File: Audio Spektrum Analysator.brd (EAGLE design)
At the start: 144.8 x 98.7 mm, 148 parts, among them IC1 LM324N, IC10 LM3914N, IC11 LM3914N, IC12 LM3914N, IC13 LM3914N, IC2 LM324N, IC3 LM324N, IC4 LM3914N, IC5 LM3914N, IC6 LM3914N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

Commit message: moved names
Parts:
- removed R8: 1k, rcl:0207/7
- removed R9: 1k, resistor:0207/7
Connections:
- removed net N$31: R10.S, R8.2
- removed net N$44: R11.S, R9.2
- net N$123: now also R11.S; no longer R9.1
- net N$5: now also R10.S; no longer R8.1
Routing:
- net N$44: track 6.88 -> 0.00 mm
- net N$31: track 6.88 -> 0.00 mm
- net N$5: track 8.15 -> 4.34 mm
- net N$123: track 6.35 -> 2.54 mm
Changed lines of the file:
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@@
 <layer number="25" name="tNames" color="7" fill="1" visible="yes" active="yes"/>
 <layer number="26" name="bNames" color="7" fill="1" visible="yes" active="yes"/>
-<layer number="27" name="tValues" color="7" fill="1" visible="yes" active="yes"/>
-<layer number="28" name="bValues" color="7" fill="1" visible="yes" active="yes"/>
+<layer number="27" name="tValues" color="7" fill="1" visible="no" active="yes"/>
+<layer number="28" name="bValues" color="7" fill="1" visible="no" active="yes"/>
 <layer number="29" name="tStop" color="7" fill="3" visible="no" active="yes"/>
 <layer number="30" name="bStop" color="7" fill="6" visible="no" active="yes"/>
@@
 <rectangle x1="134.127" y1="76.406" x2="134.787" y2="76.466" layer="26"/>
 <rectangle x1="134.127" y1="76.466" x2="134.787" y2="76.526" layer="26"/>
-<text x="1.27" y="0.762" size="1.778" layer="25" font="vector">5V</text>
+<text x="2.54" y="0.762" size="1.778" layer="25" font="vector">5V</text>
 </plain>
 <attributes>
@@
 <attribute name="VALUE" x="51.3588" y="4.064" size="1.27" layer="27" font="vector" ratio="10" rot="R90"/>
 </element>
-<element name="R9" library="resistor" library_urn="urn:adsk.eagle:library:348" package="0207/7" package3d_urn="urn:adsk.eagle:package:23493/1" value="1k" x="54.61" y="6.35" smashed="yes" rot="R270">
-<attribute name="NAME" x="55.626" y="10.922" size="1.27" layer="25" font="vector" ratio="10"/>
-<attribute name="VALUE" x="54.0512" y="8.636" size="1.27" layer="27" font="vector" ratio="10" rot="R270"/>
-</element>
 <element name="R17" library="resistor" library_urn="urn:adsk.eagle:library:348" package="0207/7" package3d_urn="urn:adsk.eagle:package:23493/1" value="1M" x="55.88" y="24.13" smashed="yes">
 <attribute name="NAME" x="53.34" y="25.527" size="1.27" layer="25" font="vector" ratio="10"/>
@@
 <attribute name="VALUE" x="107.2388" y="24.384" size="1.27" layer="27" font="vector" ratio="10" rot="R90"/>
 </element>
-<element name="R8" library="rcl" library_urn="urn:adsk.eagle:library:334" package="0207/7" package3d_urn="urn:adsk.eagle:package:23493/1" value="1k" x="34.29" y="6.35" smashed="yes" rot="R270">
-<attribute name="NAME" x="32.131" y="11.049" size="1.27" layer="25" font="vector" ratio="10"/>
-<attribute name="SPICEPREFIX" value="R" x="34.29" y="6.35" size="1.778" layer="27" rot="R270" display="off"/>
-<attribute name="VALUE" x="33.7312" y="8.636" size="1.27" layer="27" font="vector" ratio="10" rot="R270"/>
-</element>
 <element name="R47" library="resistor" library_urn="urn:adsk.eagle:library:348" package="0207/7" package3d_urn="urn:adsk.eagle:package:23493/1" value="1k2" x="43.815" y="57.15" smashed="yes" rot="R270">
 <attribute name="NAME" x="44.45" y="62.23" size="1.27" layer="25" font="vector" ratio="10" rot="R90"/>
@@
 <signal name="N$5">
 <contactref element="R6" pad="2"/>
-<contactref element="R8" pad="1"/>
 <contactref element="IC1" pad="2"/>
 <wire x1="40.64" y1="12.7" x2="40.64" y2="11.43" width="0.4064" layer="1"/>
 <wire x1="40.64" y1="11.43" x2="39.37" y2="10.16" width="0.4064" layer="1"/>
 <wire x1="39.37" y1="10.16" x2="38.1" y2="10.16" width="0.4064" layer="1"/>
-<wire x1="38.1" y1="10.16" x2="34.29" y2="10.16" width="0.4064" layer="1"/>
+<contactref element="R10" pad="S"/>
+<wire x1="27.94" y1="3.81" x2="38.1" y2="10.16" width="0" layer="19" extent="1-1"/>
 </signal>
 <signal name="N$6">
@@
 <contactref element="IC1" pad="6"/>
 <contactref element="R7" pad="2"/>
-<contactref element="R9" pad="1"/>
 <wire x1="50.8" y1="12.7" x2="50.8" y2="10.16" width="0.4064" layer="1"/>
-<wire x1="50.8" y1="10.16" x2="54.61" y2="10.16" width="0.4064" layer="1"/>
+<contactref element="R11" pad="S"/>
+<wire x1="50.8" y1="10.16" x2="60.96" y2="3.81" width="0" layer="19" extent="1-1"/>
 </signal>
 <signal name="REF">
@@
 <wire x1="20.32" y1="11.43" x2="20.32" y2="13.97" width="0.4064" layer="1"/>
 </signal>
-<signal name="N$31">
-<contactref element="R8" pad="2"/>
-<contactref element="R10" pad="S"/>
-<wire x1="27.94" y1="3.81" x2="29.21" y2="2.54" width="0.4064" layer="1"/>
-<wire x1="29.21" y1="2.54" x2="34.29" y2="2.54" width="0.4064" layer="1"/>
-</signal>
-<signal name="N$44">
-<contactref element="R9" pad="2"/>
-<contactref element="R11" pad="S"/>
-<wire x1="54.61" y1="2.54" x2="59.69" y2="2.54" width="0.4064" layer="1"/>
-<wire x1="59.69" y1="2.54" x2="60.96" y2="3.81" width="0.4064" layer="1"/>
-</signal>
 </signals>

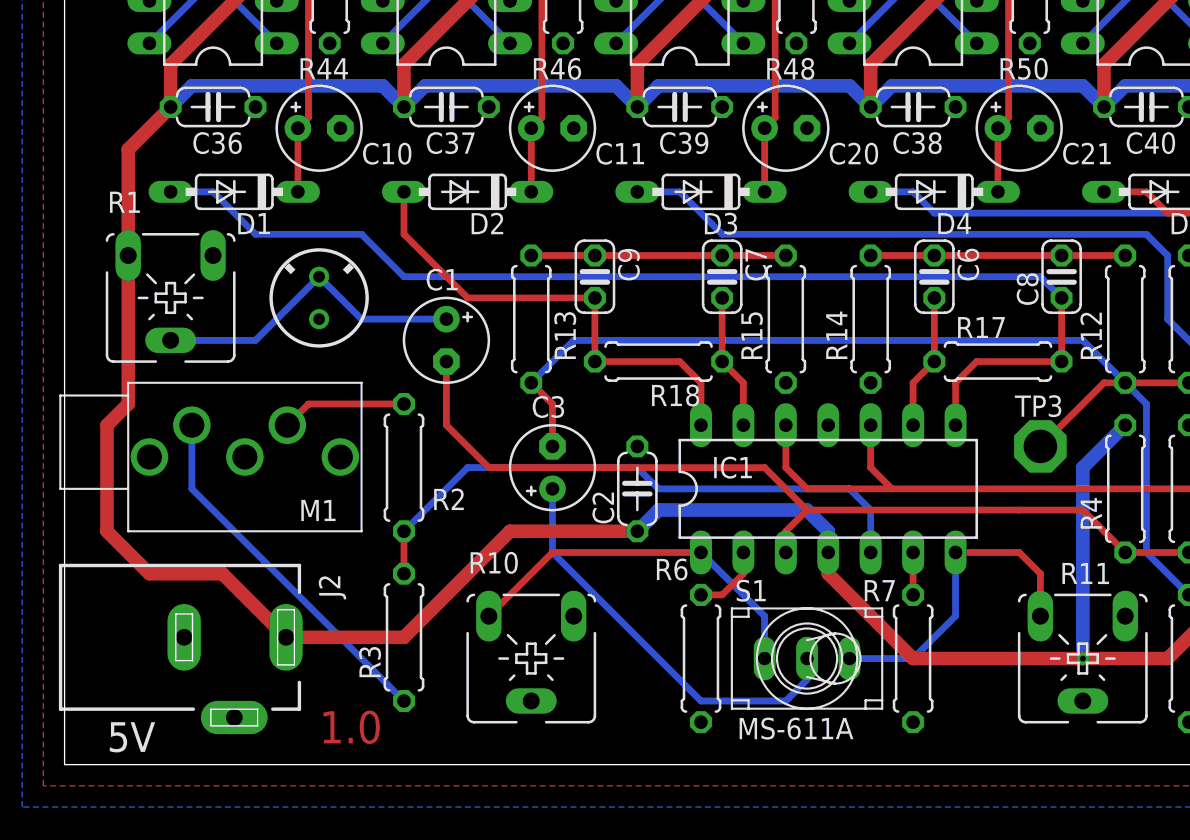
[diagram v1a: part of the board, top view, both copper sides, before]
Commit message: worked on electret mic amp
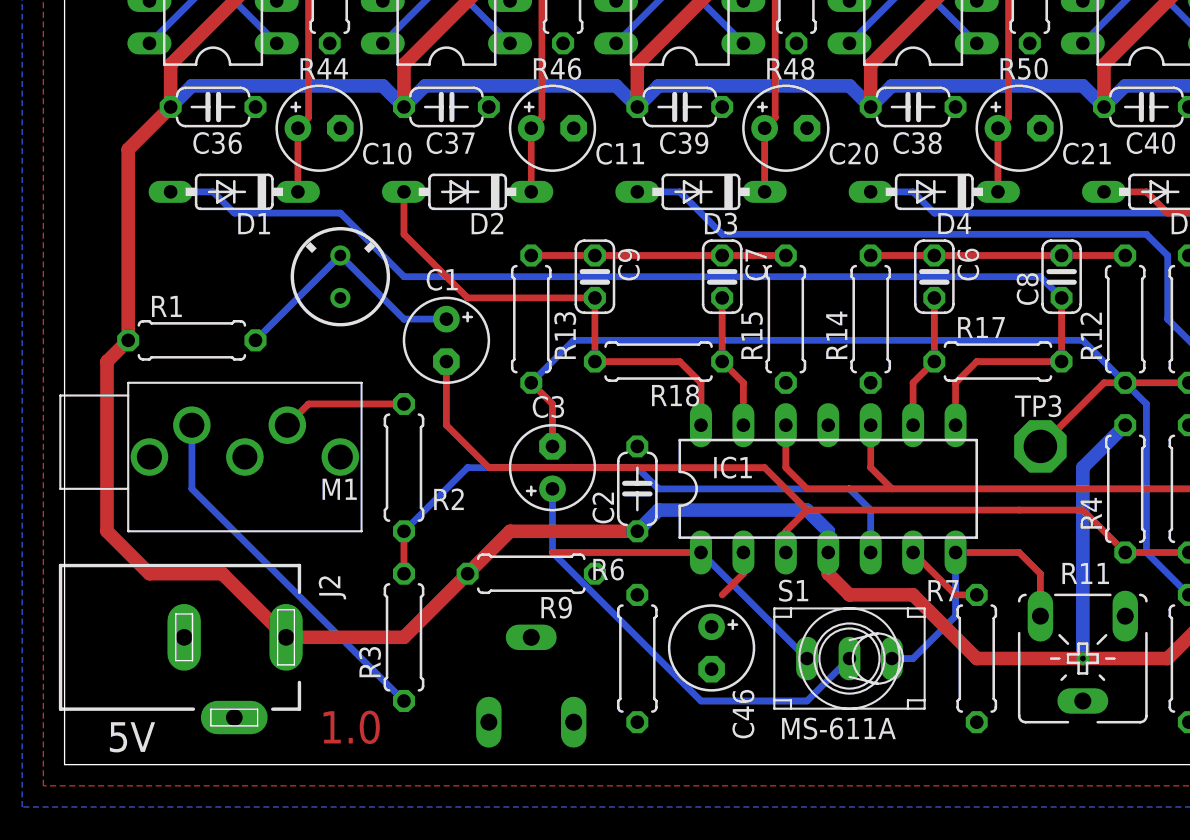
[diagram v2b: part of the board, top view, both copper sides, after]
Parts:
- removed R10: 10k, pot:CA6V
- added C46: 2u2, resistor:E2,5-5
- added R8: 10k, pot:CA6V
- added R9: 100k, rcl:0207/7
- R1: device pot:CA6V -> rcl:0207/7
- moved R6 3.81 mm to (34.3, 6.35)
- moved R7 3.81 mm to (54.6, 6.35)
- moved R1 2.84 mm to (7.62, 25.4)
- moved S1 2.54 mm to (47.0, 6.35)
- moved M1 1.80 mm to (16.5, 29.2)
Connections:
- new net N$31: C46.-, R6.2
- new net N$44: R6.1, R8.E
- net +5V: now also R1.2; no longer R1.E
- net GND: now also R8.S; no longer R6.1
- net N$13: now also R1.1; no longer R1.S
- net N$5: now also C46.+, R9.1; no longer R10.S, R6.2
- net N$6: now also R9.2; no longer R10.E
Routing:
- net N$6: track 22.2 -> 17.9 mm
- net N$13: track 19.1 -> 15.1 mm
- net N$10: track 19.4 -> 16.8 mm
- net N$123: track 2.54 -> 4.86 mm
- net N$12: track 24.5 -> 26.3 mm
- net N$5: track 4.34 -> 3.07 mm
